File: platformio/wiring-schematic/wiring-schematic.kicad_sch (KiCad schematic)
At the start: 5 parts, among them U0 LSM9DS1, U1 LSM9DS1, U2 LSM9DS1, U3 LSM9DS1

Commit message: reorganised kicad schematic
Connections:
- net +5V: no longer U0.22 (VDD), U0.23 (VDD), U1.22 (VDD), U1.23 (VDD), U2.22 (VDD), U2.23 (VDD), U3.22 (VDD), U3.23 (VDD)
- net GND: no longer U0.19 (GND), U0.20 (GND), U1.19 (GND), U1.20 (GND), U2.19 (GND), U2.20 (GND), U3.19 (GND), U3.20 (GND)
- net CS Accel IMU 0 renamed CS_A_0
- net CS Accel IMU 1 renamed CS_A_1
- net CS Accel IMU 2 renamed CS_A_2
- net CS Accel IMU 3 renamed CS_A_3
- net CS_Mag_IMU_0 renamed CS_M_0
- net CS_Mag_IMU_1 renamed CS_M_1
- net CS_Mag_IMU_2 renamed CS_M_2
- net CS_Mag_IMU_3 renamed CS_M_3
- new net: U0.19 (GND), U0.20 (GND)
- new net: U3.19 (GND), U3.20 (GND)
- new net: U2.19 (GND), U2.20 (GND)
- new net: U1.19 (GND), U1.20 (GND)
- new net VDD: U0.22 (VDD), U0.23 (VDD), U1.22 (VDD), U1.23 (VDD), U2.22 (VDD), U2.23 (VDD), U3.22 (VDD), U3.23 (VDD)
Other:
- note removed: "SPI_MISO"

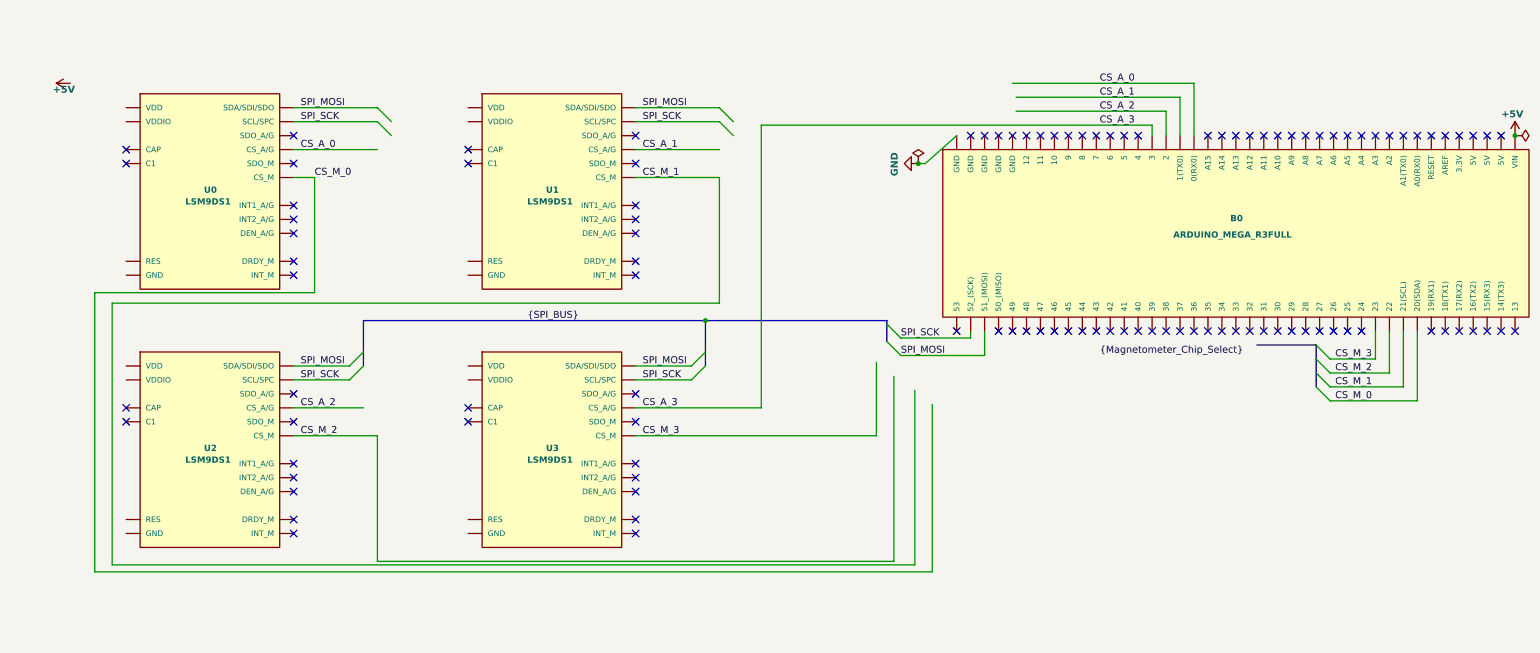
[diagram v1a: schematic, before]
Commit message: Finalised kicad schematic, and exported SVG
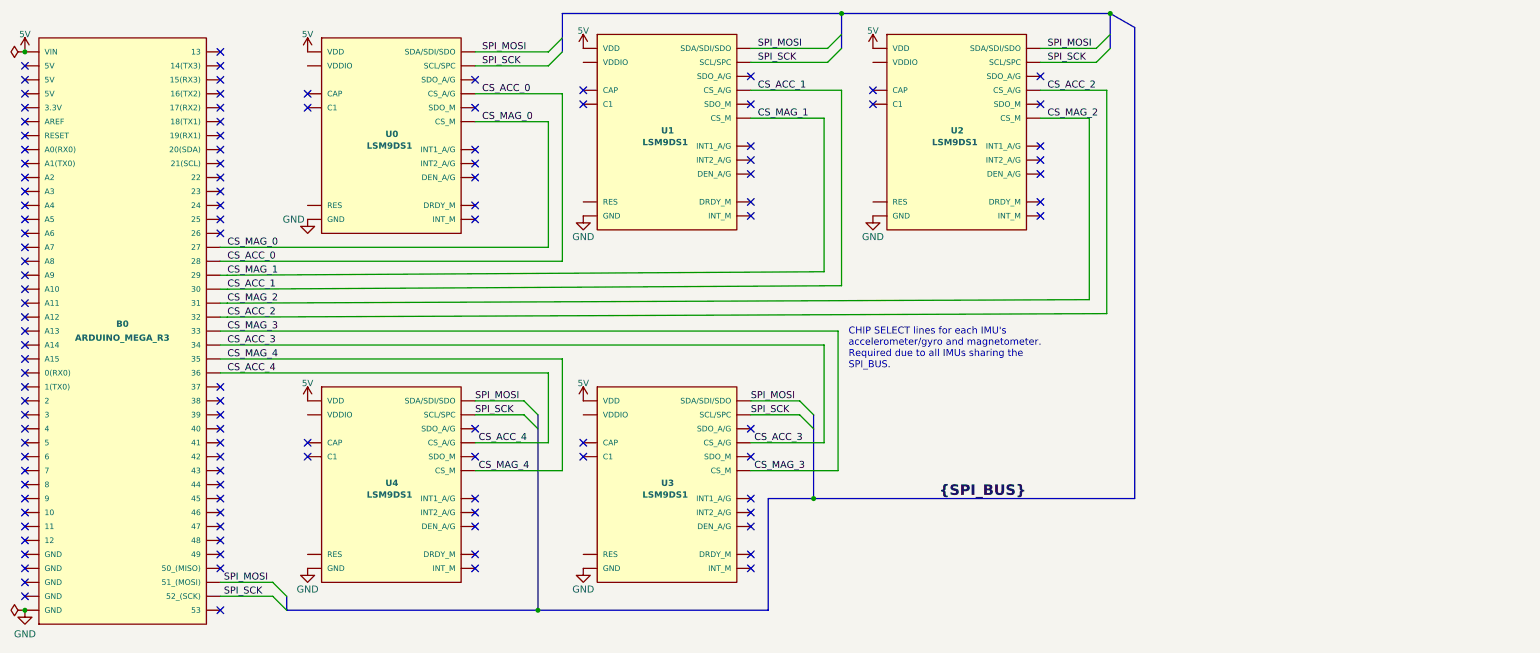
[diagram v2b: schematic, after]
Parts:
- added U3: LSM9DS1, LGA-24-3.5X3, symbol SparkFun-Sensors:LSM9DS1
- B0: value ARDUINO_MEGA_R3FULL -> ARDUINO_MEGA_R3
- renumbered U3 to U4
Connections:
- net VDD is gone; now on net 5V: U0.22 (VDD), U0.23 (VDD), U1.22 (VDD), U1.23 (VDD), U2.22 (VDD), U2.23 (VDD), U4.22 (VDD), U4.23 (VDD)
- net GND: now also U0.19 (GND), U0.20 (GND), U1.19 (GND), U1.20 (GND), U2.19 (GND), U2.20 (GND), U4.19 (GND), U4.20 (GND), U3.19 (GND), U3.20 (GND)
- net SPI_MOSI: now also U3.4 (SDA/SDI/SDO)
- net SPI_SCK: now also U3.2 (SCL/SPC)
- net CS_MAG_0: now reaches B0.27
- net CS_MAG_0: now also U0.8 (CS_M)
- net CS_ACC_0: now reaches B0.28
- net CS_ACC_0: now also U0.7 (CS_A/G)
- net CS_MAG_1: now reaches B0.29
- net CS_MAG_1: now also U1.8 (CS_M)
- net CS_ACC_1: now reaches B0.30
- net CS_ACC_1: now also U1.7 (CS_A/G)
- net CS_MAG_2: now reaches B0.31
- net CS_MAG_2: now also U2.8 (CS_M)
- net CS_ACC_2: now reaches B0.32
- net CS_ACC_2: now also U2.7 (CS_A/G)
- net CS_MAG_3: now reaches B0.33
- net CS_MAG_3: now also U3.8 (CS_M)
- net CS_ACC_3: now reaches B0.34
- net CS_ACC_3: now also U3.7 (CS_A/G)
- net CS_MAG_4: now reaches B0.35
- net CS_MAG_4: now also U4.8 (CS_M)
- net CS_ACC_4: now reaches B0.36
- net CS_ACC_4: now also U4.7 (CS_A/G)
- net +5V renamed 5V
- net 5V: now also U3.22 (VDD), U3.23 (VDD)
- net CS_A_0: no longer names the net of B0.0 (0(RX0))
- net CS_A_0: no longer U0.7 (CS_A/G)
- net CS_A_1: no longer names the net of B0.1 (1(TX0))
- net CS_A_1: no longer U1.7 (CS_A/G)
- net CS_A_2: no longer names the net of B0.2
- net CS_A_2: no longer U2.7 (CS_A/G)
- net CS_A_3: no longer names the net of B0.3
- net CS_A_3: no longer U4.7 (CS_A/G)
- net CS_M_0: no longer names the net of B0.20 (20(SDA))
- net CS_M_0: no longer U0.8 (CS_M)
- net CS_M_1: no longer names the net of B0.21 (21(SCL))
- net CS_M_1: no longer U1.8 (CS_M)
- net CS_M_2: no longer names the net of B0.22
- net CS_M_2: no longer U2.8 (CS_M)
- net CS_M_3: no longer names the net of B0.23
- net CS_M_3: no longer U4.8 (CS_M)
- new net: U3.1 (VDDIO), U3.3 (VDDIO)
- new net: U3.14 (RES), U3.15 (RES), U3.16 (RES), U3.17 (RES), U3.18 (RES)
- no-connect marks 106 -> 113
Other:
- note added: "CHIP SELECT lines for each IMU's accelerometer/gyro and magnetometer. Required due to all IMUs sharing the SPI_BUS."
- moved on the sheet: B0, U0, U1, U2, U4

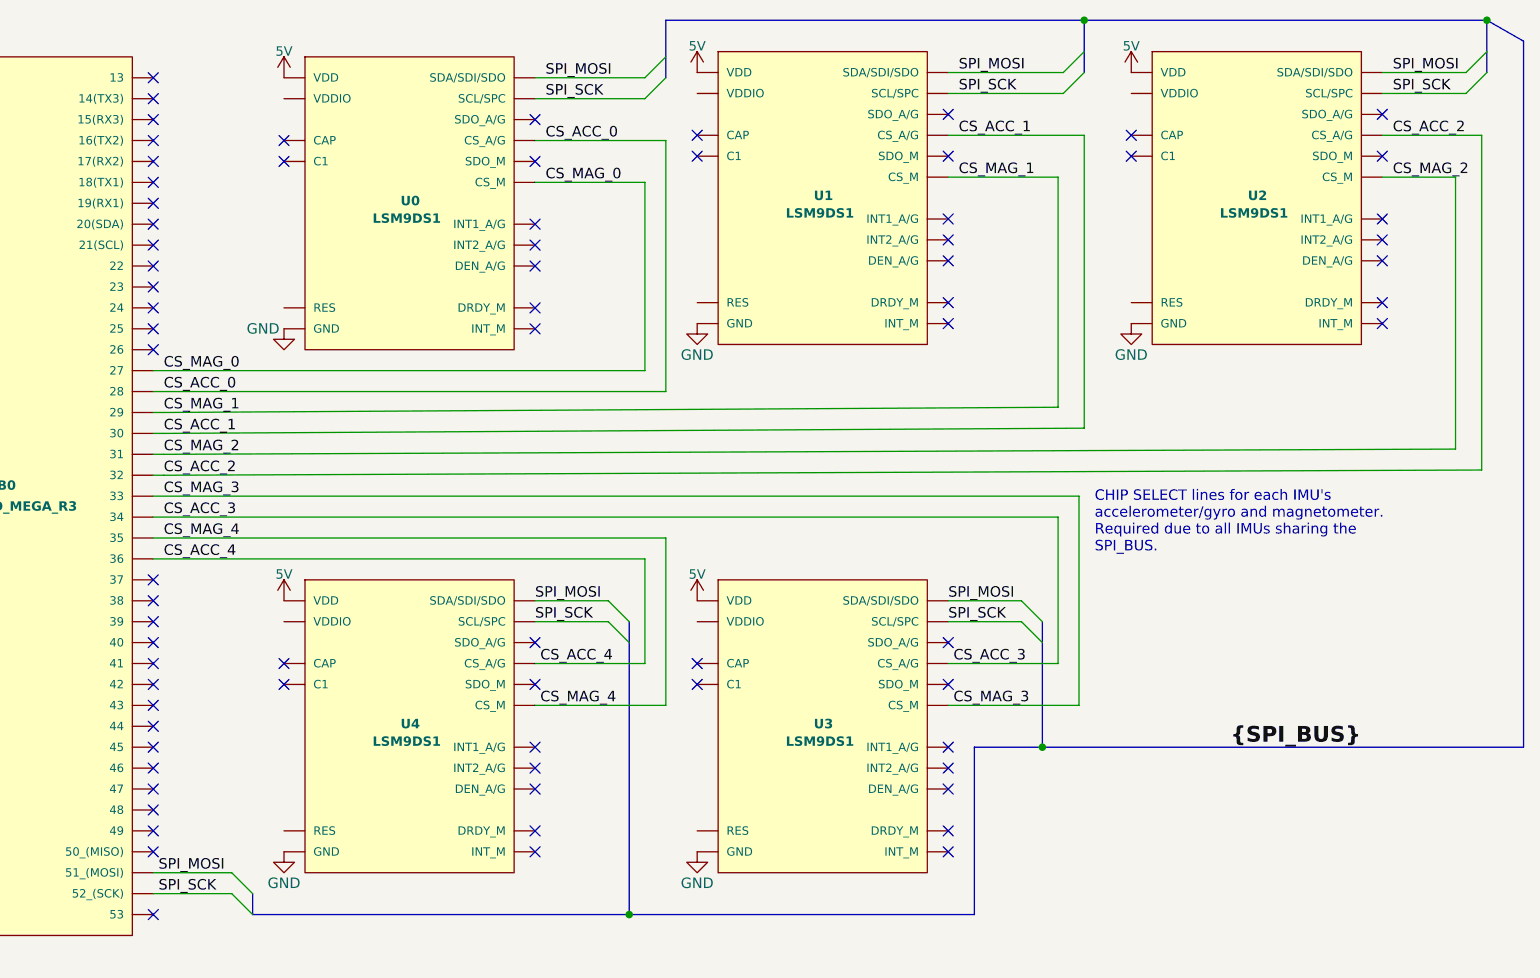
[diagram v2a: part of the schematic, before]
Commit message: Updated kicad schematic to include missing MISO line
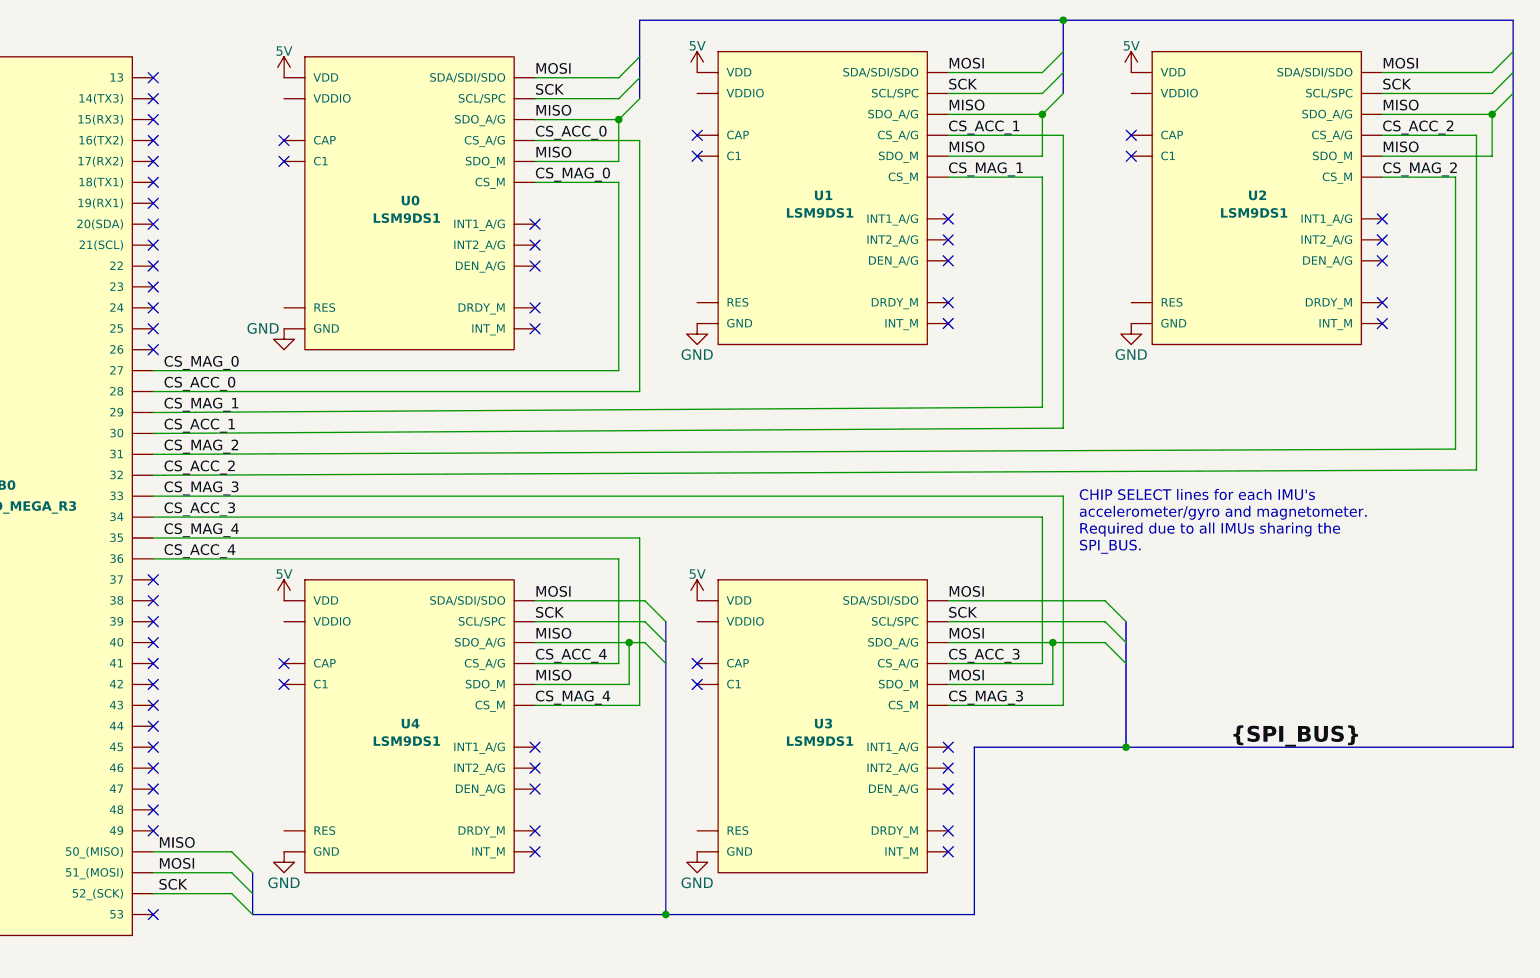
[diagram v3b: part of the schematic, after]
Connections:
- net SPI_MOSI is gone; now on net MOSI: B0.51 (51_(MOSI)), U0.4 (SDA/SDI/SDO), U1.4 (SDA/SDI/SDO), U2.4 (SDA/SDI/SDO), U3.4 (SDA/SDI/SDO), U4.4 (SDA/SDI/SDO)
- net MISO: now reaches U0.5 (SDO_A/G)
- net MISO: now also B0.50 (50_(MISO)), U0.6 (SDO_M), U1.5 (SDO_A/G), U1.6 (SDO_M), U2.5 (SDO_A/G), U2.6 (SDO_M), U4.5 (SDO_A/G), U4.6 (SDO_M)
- net MOSI: now reaches U3.5 (SDO_A/G)
- net MOSI: now also U3.6 (SDO_M)
- net SPI_SCK renamed SCK
- no-connect marks 113 -> 102

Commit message: Added fake SLDP company name to kicad schematic
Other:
- company: (none) -> EZ-TRAK INC.
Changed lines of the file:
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@@
     (date "2021-04-05")
     (rev "0.1.1")
+    (company "EZ-TRAK INC.")
     (comment 1 "Schematic for IMU sensor wiring to Arduino Mega.")
     (comment 2 "Five IMUs are shown here. ")

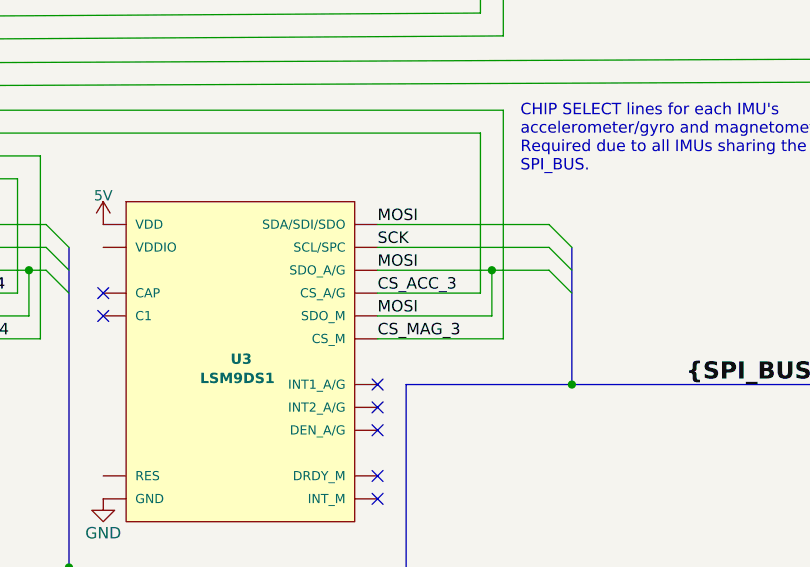
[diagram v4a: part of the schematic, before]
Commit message: Removed fritzing diagramme & updated kicad info
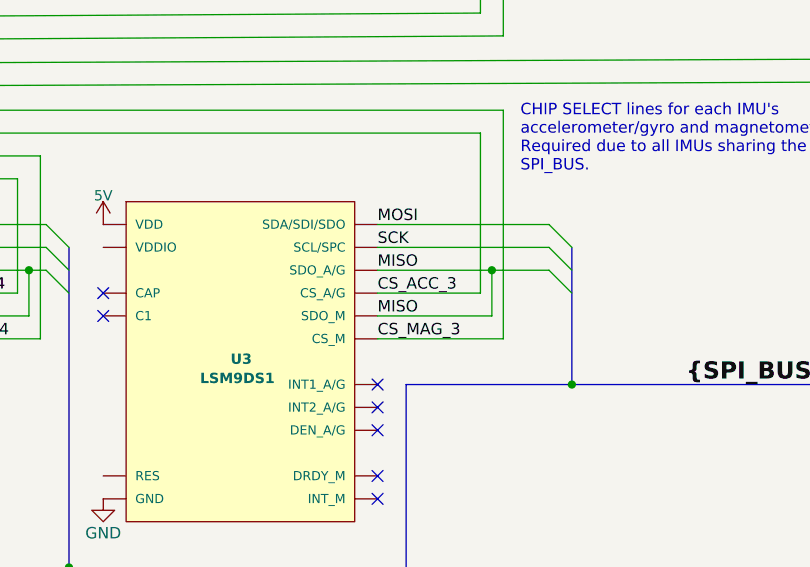
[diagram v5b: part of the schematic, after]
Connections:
- net MISO: now also U3.5 (SDO_A/G), U3.6 (SDO_M)
- net MOSI: no longer U3.5 (SDO_A/G), U3.6 (SDO_M)
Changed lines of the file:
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@@
     (title "Track-O-Tron 5000")
     (date "2021-04-05")
-    (rev "0.1.1")
+    (rev "0.3.1")
     (company "EZ-TRAK INC.")
     (comment 1 "Schematic for IMU sensor wiring to Arduino Mega.")
@@
     (effects (font (size 1.27 1.27)) (justify left bottom))
   )
-  (label "MOSI" (at 139.7 79.375 0)
+  (label "MISO" (at 139.7 79.375 0)
     (effects (font (size 1.27 1.27)) (justify left bottom))
   )
@@
     (effects (font (size 1.27 1.27)) (justify left bottom))
   )
-  (label "MOSI" (at 139.7 84.455 0)
-    (effects (font (size 1.27 1.27)) (justify left bottom))
-  )
+  (label "MISO" (at 139.7 84.455 0)
+    (effects (font (size 1.27 1.27)) (justify left bottom))
+  )
